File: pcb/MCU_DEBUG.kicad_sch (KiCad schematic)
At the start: 1 part

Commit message: add footprints
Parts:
- gave numbers to parts that had none: 1
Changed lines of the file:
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@@
   (symbol (lib_id "power:GND") (at 106.68 102.87 0) (unit 1)
     (in_bom yes) (on_board yes) (fields_autoplaced)
-    (property "Reference" "#PWR?" (id 0) (at 106.68 109.22 0)
+    (property "Reference" "#PWR0902" (id 0) (at 106.68 109.22 0)
       (effects (font (size 1.27 1.27)) hide)
     )
@@
   (symbol (lib_id "power:+3.3V") (at 106.68 86.36 0) (unit 1)
     (in_bom yes) (on_board yes) (fields_autoplaced)
-    (property "Reference" "#PWR?" (id 0) (at 106.68 90.17 0)
+    (property "Reference" "#PWR0901" (id 0) (at 106.68 90.17 0)
       (effects (font (size 1.27 1.27)) hide)
     )
@@
   (symbol (lib_id "datamaskin:mcu_debug") (at 116.84 100.33 0) (unit 1)
     (in_bom yes) (on_board yes) (fields_autoplaced)
-    (property "Reference" "J?" (id 0) (at 116.84 82.55 0))
+    (property "Reference" "J901" (id 0) (at 116.84 82.55 0))
     (property "Value" "mcu_debug" (id 1) (at 116.84 85.09 0))
     (property "Footprint" "" (id 2) (at 116.84 100.33 0)

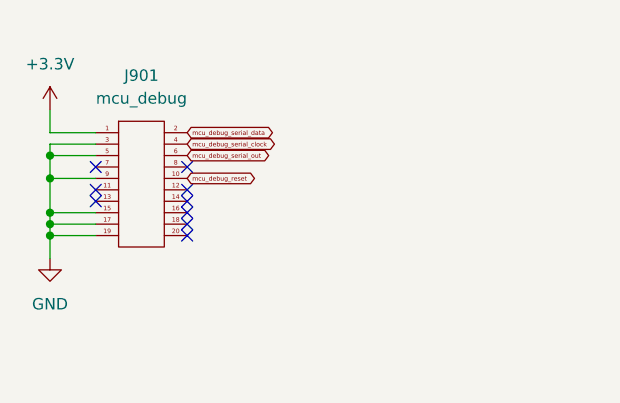
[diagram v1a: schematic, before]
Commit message: add footprints + fix unnconnected
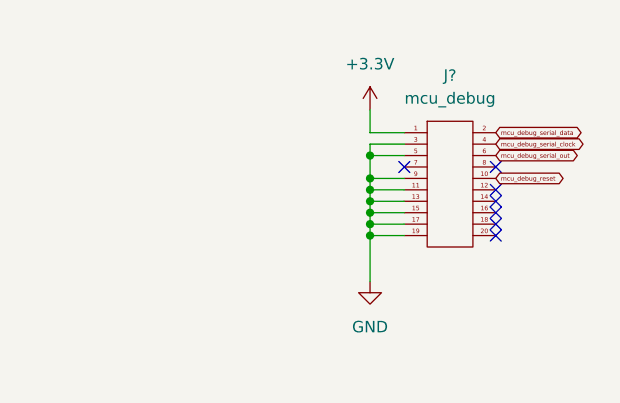
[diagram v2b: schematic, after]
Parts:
- removed J901: mcu_debug, symbol datamaskin:mcu_debug
- added J?: mcu_debug, debug-footprints:SAMTEC_FTSH-110-01-L-DV-007, symbol Carl_symboler:mcu_debug
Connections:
- net +3.3V: now also J?.1
- net GND: now also J?.11, J?.13, J?.15, J?.17, J?.19, J?.3, J?.5, J?.9
- net mcu_debug_reset: now also J?.10
- net mcu_debug_serial_clock: now also J?.4
- net mcu_debug_serial_data: now also J?.2
- net mcu_debug_serial_out: now also J?.6
- no-connect marks 9 -> 7
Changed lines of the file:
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@@
 (kicad_sch (version 20211123) (generator eeschema)
   (paper "A4")
-  (junction (at 106.68 99.06) (diameter 0) (color 0 0 0 0)
+  (junction (at 142.24 95.25) (diameter 0) (color 0 0 0 0)
   )
-  (junction (at 106.68 100.33) (diameter 0) (color 0 0 0 0)
+  (junction (at 142.24 93.98) (diameter 0) (color 0 0 0 0)
   )
-  (junction (at 106.68 97.79) (diameter 0) (color 0 0 0 0)
+  (junction (at 142.24 96.52) (diameter 0) (color 0 0 0 0)
   )
-  (junction (at 106.68 93.98) (diameter 0) (color 0 0 0 0)
+  (junction (at 142.24 99.06) (diameter 0) (color 0 0 0 0)
   )
-  (junction (at 106.68 91.44) (diameter 0) (color 0 0 0 0)
+  (junction (at 142.24 97.79) (diameter 0) (color 0 0 0 0)
   )
-  (no_connect (at 121.92 97.79))
-  (no_connect (at 121.92 95.25))
-  (no_connect (at 121.92 100.33))
-  (no_connect (at 121.92 92.71))
-  (no_connect (at 111.76 92.71))
-  (no_connect (at 111.76 95.25))
-  (no_connect (at 121.92 96.52))
-  (no_connect (at 111.76 96.52))
-  (no_connect (at 121.92 99.06))
-  (wire (pts (xy 106.68 90.17) (xy 111.76 90.17))
+  (junction (at 142.24 100.33) (diameter 0) (color 0 0 0 0)
+  )
+  (junction (at 142.24 91.44) (diameter 0) (color 0 0 0 0)
+  )
+  (no_connect (at 156.21 96.52))
+  (no_connect (at 156.21 100.33))
+  (no_connect (at 146.05 92.71))
+  (no_connect (at 156.21 99.06))
+  (no_connect (at 156.21 97.79))
+  (no_connect (at 156.21 92.71))
+  (no_connect (at 156.21 95.25))
+  (wire (pts (xy 142.24 96.52) (xy 146.05 96.52))
     (stroke (width 0) (type default) (color 0 0 0 0))
   )
-  (wire (pts (xy 106.68 100.33) (xy 106.68 102.87))
+  (wire (pts (xy 142.24 97.79) (xy 142.24 99.06))
     (stroke (width 0) (type default) (color 0 0 0 0))
   )
-  (wire (pts (xy 106.68 100.33) (xy 111.76 100.33))
+  (wire (pts (xy 146.05 88.9) (xy 142.24 88.9))
     (stroke (width 0) (type default) (color 0 0 0 0))
   )
-  (wire (pts (xy 106.68 97.79) (xy 106.68 99.06))
+  (wire (pts (xy 142.24 88.9) (xy 142.24 86.36))
     (stroke (width 0) (type default) (color 0 0 0 0))
   )
-  (wire (pts (xy 106.68 99.06) (xy 111.76 99.06))
+  (wire (pts (xy 142.24 96.52) (xy 142.24 97.79))
     (stroke (width 0) (type default) (color 0 0 0 0))
   )
-  (wire (pts (xy 106.68 97.79) (xy 111.76 97.79))
+  (wire (pts (xy 142.24 95.25) (xy 146.05 95.25))
     (stroke (width 0) (type default) (color 0 0 0 0))
   )
-  (wire (pts (xy 106.68 93.98) (xy 106.68 97.79))
+  (wire (pts (xy 142.24 99.06) (xy 146.05 99.06))
     (stroke (width 0) (type default) (color 0 0 0 0))
   )
-  (wire (pts (xy 106.68 90.17) (xy 106.68 91.44))
+  (wire (pts (xy 142.24 91.44) (xy 142.24 93.98))
     (stroke (width 0) (type default) (color 0 0 0 0))
   )
-  (wire (pts (xy 106.68 99.06) (xy 106.68 100.33))
+  (wire (pts (xy 142.24 95.25) (xy 142.24 96.52))
     (stroke (width 0) (type default) (color 0 0 0 0))
   )
-  (wire (pts (xy 106.68 91.44) (xy 106.68 93.98))
+  (wire (pts (xy 142.24 99.06) (xy 142.24 100.33))
     (stroke (width 0) (type default) (color 0 0 0 0))
   )
-  (wire (pts (xy 106.68 91.44) (xy 111.76 91.44))
+  (wire (pts (xy 142.24 90.17) (xy 142.24 91.44))
     (stroke (width 0) (type default) (color 0 0 0 0))
   )
-  (wire (pts (xy 106.68 88.9) (xy 106.68 86.36))
+  (wire (pts (xy 142.24 93.98) (xy 142.24 95.25))
     (stroke (width 0) (type default) (color 0 0 0 0))
   )
-  (wire (pts (xy 106.68 93.98) (xy 111.76 93.98))
+  (wire (pts (xy 142.24 93.98) (xy 146.05 93.98))
     (stroke (width 0) (type default) (color 0 0 0 0))
   )
-  (wire (pts (xy 106.68 88.9) (xy 111.76 88.9))
+  (wire (pts (xy 142.24 91.44) (xy 146.05 91.44))
     (stroke (width 0) (type default) (color 0 0 0 0))
   )
-  (global_label "mcu_debug_serial_data" (shape bidirectional) (at 121.92 88.9 0) (fields_autoplaced)
+  (wire (pts (xy 142.24 97.79) (xy 146.05 97.79))
+    (stroke (width 0) (type default) (color 0 0 0 0))
+  )
+  (wire (pts (xy 142.24 100.33) (xy 146.05 100.33))
+    (stroke (width 0) (type default) (color 0 0 0 0))
+  )
+  (wire (pts (xy 146.05 90.17) (xy 142.24 90.17))
+    (stroke (width 0) (type default) (color 0 0 0 0))
+  )
+  (wire (pts (xy 142.24 100.33) (xy 142.24 105.41))
+    (stroke (width 0) (type default) (color 0 0 0 0))
+  )
+  (global_label "mcu_debug_serial_out" (shape bidirectional) (at 156.21 91.44 0) (fields_autoplaced)
     (effects (font (size 0.5 0.5)) (justify left))
-    (property "Intersheet References" "${INTERSHEET_REFS}" (id 0) (at 131.5367 88.8688 0)
+    (property "Intersheet References" "${INTERSHEET_REFS}" (id 0) (at 165.3743 91.4088 0)
       (effects (font (size 0.5 0.5)) (justify left) hide)
     )
   )
-  (global_label "mcu_debug_serial_out" (shape bidirectional) (at 121.92 91.44 0) (fields_autoplaced)
+  (global_label "mcu_debug_reset" (shape bidirectional) (at 156.21 93.98 0) (fields_autoplaced)
     (effects (font (size 0.5 0.5)) (justify left))
-    (property "Intersheet References" "${INTERSHEET_REFS}" (id 0) (at 131.0843 91.4088 0)
+    (property "Intersheet References" "${INTERSHEET_REFS}" (id 0) (at 163.5648 93.9488 0)
       (effects (font (size 0.5 0.5)) (justify left) hide)
     )
   )
-  (global_label "mcu_debug_serial_clock" (shape bidirectional) (at 121.92 90.17 0) (fields_autoplaced)
+  (global_label "mcu_debug_serial_clock" (shape bidirectional) (at 156.21 90.17 0) (fields_autoplaced)
     (effects (font (size 0.5 0.5)) (justify left))
-    (property "Intersheet References" "${INTERSHEET_REFS}" (id 0) (at 131.87 90.1388 0)
+    (property "Intersheet References" "${INTERSHEET_REFS}" (id 0) (at 166.16 90.1388 0)
       (effects (font (size 0.5 0.5)) (justify left) hide)
     )
   )
-  (global_label "mcu_debug_reset" (shape bidirectional) (at 121.92 93.98 0) (fields_autoplaced)
+  (global_label "mcu_debug_serial_data" (shape bidirectional) (at 156.21 88.9 0) (fields_autoplaced)
     (effects (font (size 0.5 0.5)) (justify left))
-    (property "Intersheet References" "${INTERSHEET_REFS}" (id 0) (at 129.2748 93.9488 0)
+    (property "Intersheet References" "${INTERSHEET_REFS}" (id 0) (at 165.8267 88.8688 0)
       (effects (font (size 0.5 0.5)) (justify left) hide)
     )
   )
-  (symbol (lib_id "power:GND") (at 106.68 102.87 0) (unit 1)
+  (symbol (lib_id "Carl_symboler:mcu_debug") (at 151.13 100.33 0) (unit 1)
     (in_bom yes) (on_board yes) (fields_autoplaced)
-    (property "Reference" "#PWR0902" (id 0) (at 106.68 109.22 0)
+    (property "Reference" "J?" (id 0) (at 151.13 82.55 0))
+    (property "Value" "mcu_debug" (id 1) (at 151.13 85.09 0))
+    (property "Footprint" "debug-footprints:SAMTEC_FTSH-110-01-L-DV-007" (id 2) (at 151.13 100.33 0)
       (effects (font (size 1.27 1.27)) hide)
     )
-    (property "Value" "GND" (id 1) (at 106.68 107.95 0))
-    (property "Footprint" "" (id 2) (at 106.68 102.87 0)
-      (effects (font (size 1.27 1.27)) hide)
-    )
-    (property "Datasheet" "" (id 3) (at 106.68 102.87 0)
-      (effects (font (size 1.27 1.27)) hide)
-    )
-    (pin "1")
-  )
-  (symbol (lib_id "power:+3.3V") (at 106.68 86.36 0) (unit 1)
-    (in_bom yes) (on_board yes) (fields_autoplaced)
-    (property "Reference" "#PWR0901" (id 0) (at 106.68 90.17 0)
-      (effects (font (size 1.27 1.27)) hide)
-    )
-    (property "Value" "+3.3V" (id 1) (at 106.68 81.28 0))
-    (property "Footprint" "" (id 2) (at 106.68 86.36 0)
-      (effects (font (size 1.27 1.27)) hide)
-    )
-    (property "Datasheet" "" (id 3) (at 106.68 86.36 0)
-      (effects (font (size 1.27 1.27)) hide)
-    )
-    (pin "1")
-  )
-  (symbol (lib_id "datamaskin:mcu_debug") (at 116.84 100.33 0) (unit 1)
-    (in_bom yes) (on_board yes) (fields_autoplaced)
-    (property "Reference" "J901" (id 0) (at 116.84 82.55 0))
-    (property "Value" "mcu_debug" (id 1) (at 116.84 85.09 0))
-    (property "Footprint" "" (id 2) (at 116.84 100.33 0)
-      (effects (font (size 1.27 1.27)) hide)
-    )
-    (property "Datasheet" "" (id 3) (at 116.84 100.33 0)
+    (property "Datasheet" "" (id 3) (at 151.13 100.33 0)
       (effects (font (size 1.27 1.27)) hide)
     )
@@
     (pin "9")
   )
+  (symbol (lib_id "power:GND") (at 142.24 105.41 0) (unit 1)
+    (in_bom yes) (on_board yes) (fields_autoplaced)
+    (property "Reference" "#PWR0103" (id 0) (at 142.24 111.76 0)
+      (effects (font (size 1.27 1.27)) hide)
+    )
+    (property "Value" "GND" (id 1) (at 142.24 110.49 0))
+    (property "Footprint" "" (id 2) (at 142.24 105.41 0)
+      (effects (font (size 1.27 1.27)) hide)
+    )
+    (property "Datasheet" "" (id 3) (at 142.24 105.41 0)
+      (effects (font (size 1.27 1.27)) hide)
+    )
+    (pin "1")
+  )
+  (symbol (lib_id "power:+3.3V") (at 142.24 86.36 0) (unit 1)
+    (in_bom yes) (on_board yes) (fields_autoplaced)
+    (property "Reference" "#PWR0102" (id 0) (at 142.24 90.17 0)
+      (effects (font (size 1.27 1.27)) hide)
+    )
+    (property "Value" "+3.3V" (id 1) (at 142.24 81.28 0))
+    (property "Footprint" "" (id 2) (at 142.24 86.36 0)
+      (effects (font (size 1.27 1.27)) hide)
+    )
+    (property "Datasheet" "" (id 3) (at 142.24 86.36 0)
+      (effects (font (size 1.27 1.27)) hide)
+    )
+    (pin "1")
+  )
 )

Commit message: start layout
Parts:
- gave numbers to parts that had none: 1
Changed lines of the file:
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@@
   (symbol (lib_id "Carl_symboler:mcu_debug") (at 151.13 100.33 0) (unit 1)
     (in_bom yes) (on_board yes) (fields_autoplaced)
-    (property "Reference" "J?" (id 0) (at 151.13 82.55 0))
+    (property "Reference" "J1" (id 0) (at 151.13 82.55 0))
     (property "Value" "mcu_debug" (id 1) (at 151.13 85.09 0))
     (property "Footprint" "debug-footprints:SAMTEC_FTSH-110-01-L-DV-007" (id 2) (at 151.13 100.33 0)
